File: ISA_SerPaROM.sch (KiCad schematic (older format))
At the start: 93 parts, among them J1 ISA BUS, J10 Parallel Port, J11 Serial 4 IDC, J12 Serial 3 IDC, J13 UART4_SEL, J14 ROM Config, J15 LED Bar, J2 ADDR_IRQ, J3 UART1_SEL, J4 UART2_SEL, J5 ADDR, J6 Serial 2 IDC, J7 Serial 1 DB9, J8 UART3_SEL, J9 Parport IRQ Select, U1 74HCT138, U11 74LS30, U12 74LS86, U13 74LS02, U14 74LS155, U15 74LS245, U16 74LS174, U17 74LS374, U18 74LS05, U19 74LS125, U2 74HCT138, U20 74LS240, U21 74LS244, U23 16C554, U24 74HCT32, U25 GD75232N, U26 GD75232N, U27 SST39SF040, U28 74HCT688, U5 GD75232N, U6 GD75232N, X1 1.8432Mhz

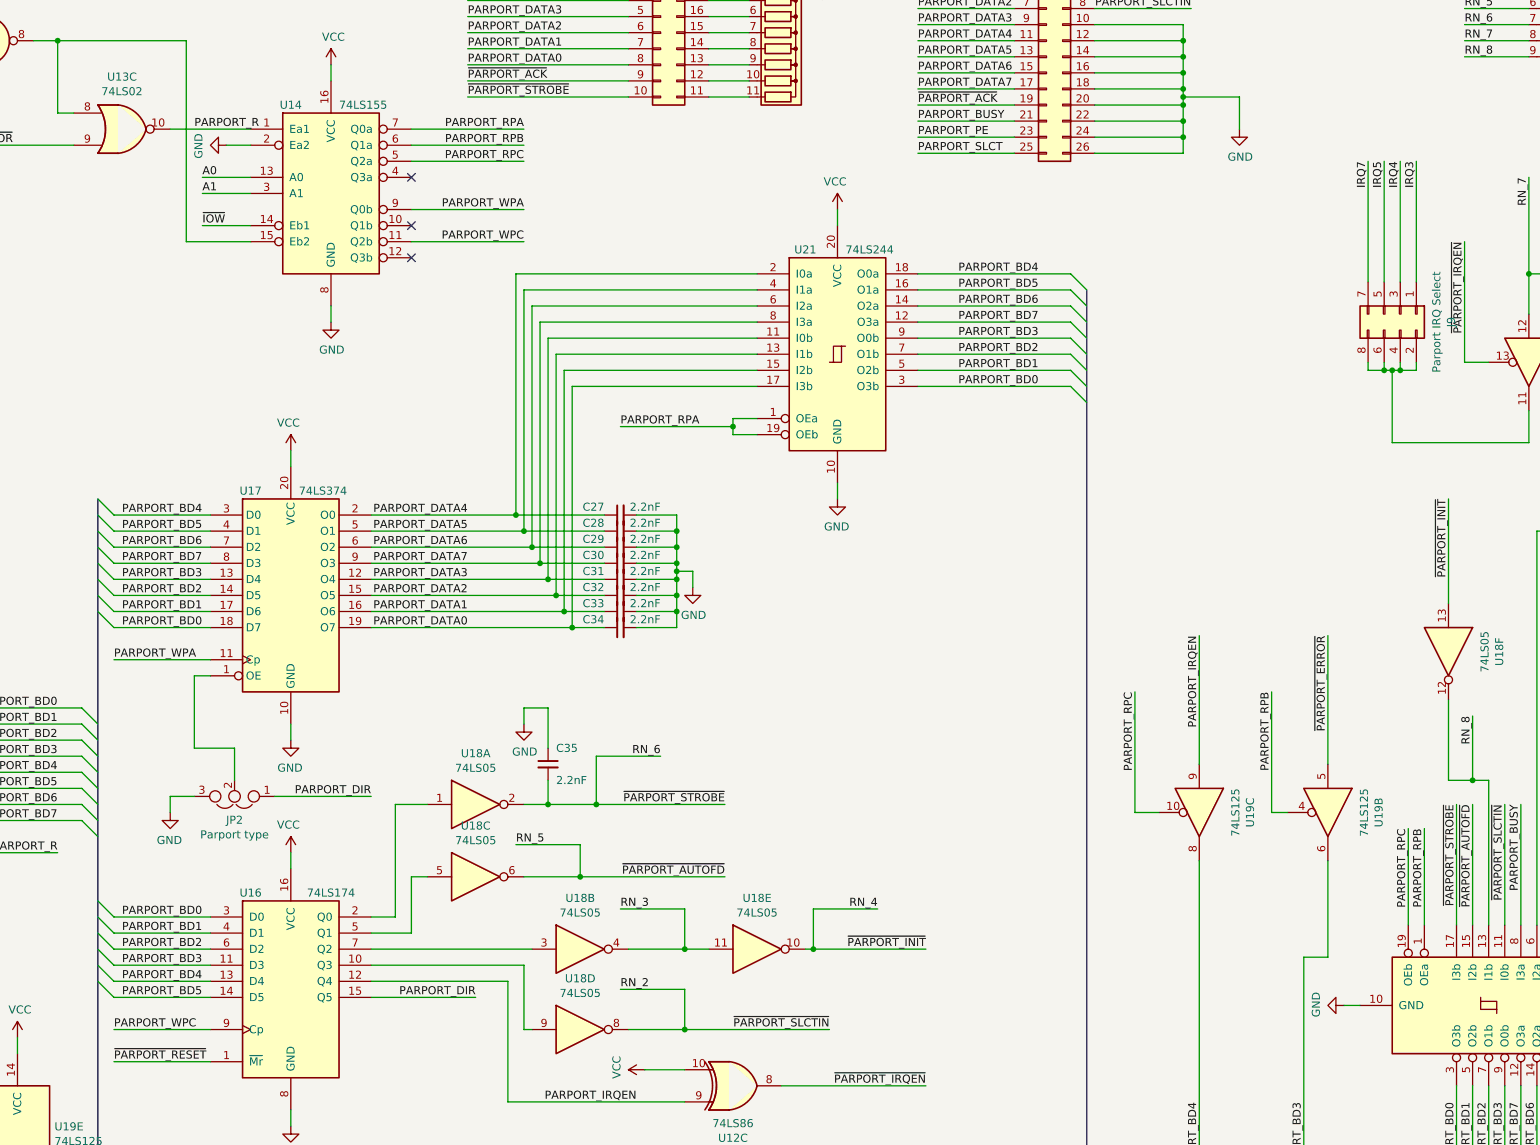
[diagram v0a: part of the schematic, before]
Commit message: Mark some active low signals as such in parport
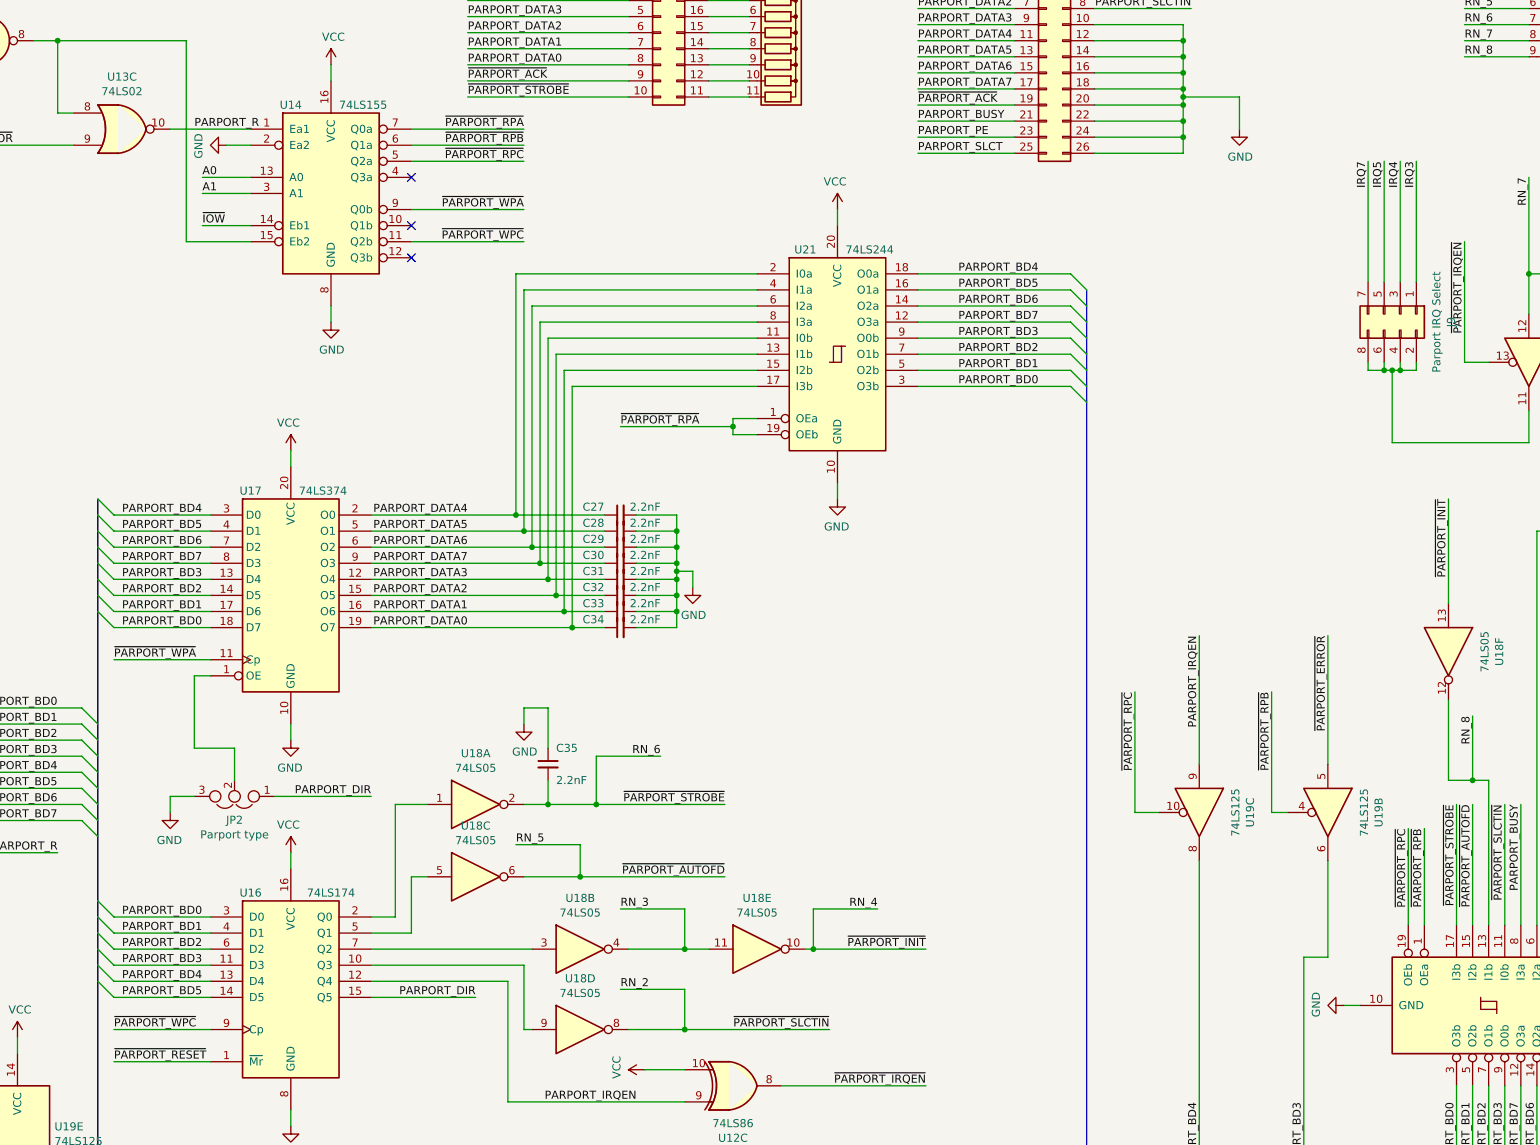
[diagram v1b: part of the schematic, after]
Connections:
- net PARPORT_RPA renamed ~PARPORT_RPA
- net PARPORT_RPB renamed ~PARPORT_RPB
- net PARPORT_RPC renamed ~PARPORT_RPC
- net PARPORT_WPA renamed ~PARPORT_WPA
- net PARPORT_WPC renamed ~PARPORT_WPC
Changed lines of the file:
@@
 NoConn ~ 9600 7600
 Text Label 10300 6800 2    50   ~ 0
-PARPORT_RPA
+~PARPORT_RPA
 Text Label 10300 6900 2    50   ~ 0
-PARPORT_RPB
+~PARPORT_RPB
 Text Label 10300 7000 2    50   ~ 0
-PARPORT_RPC
+~PARPORT_RPC
 Text Label 10300 7300 2    50   ~ 0
-PARPORT_WPA
+~PARPORT_WPA
 Text Label 10300 7500 2    50   ~ 0
-PARPORT_WPC
+~PARPORT_WPC
 $Comp
 L 74xx:74LS02 U13
@@
 	8350 12400 7750 12400
 Text Label 7750 12400 0    50   ~ 0
-PARPORT_WPC
+~PARPORT_WPC
 Wire Wire Line
 	6300 8100 6950 8100
@@
 	8350 10100 7750 10100
 Text Label 7750 10100 0    50   ~ 0
-PARPORT_WPA
+~PARPORT_WPA
 $Comp
 L Device:Jumper_NC_Dual JP2
@@
 	15900 11750 15900 11150
 Text Label 15900 11150 3    50   ~ 0
-PARPORT_RPB
+~PARPORT_RPB
 Wire Wire Line
 	15800 11750 15800 11150
 Text Label 15800 11150 3    50   ~ 0
-PARPORT_RPC
+~PARPORT_RPC
 $Comp
 L power:GND #PWR0198
@@
 	15150 13400 15050 13500
 Text Label 14950 10300 3    50   ~ 0
-PARPORT_RPB
+~PARPORT_RPB
 Wire Wire Line
 	14950 11050 15050 11050
@@
 	11600 8650 11600 8700
 Text Label 10900 8650 0    50   ~ 0
-PARPORT_RPA
+~PARPORT_RPA
 Wire Wire Line
 	12750 8400 13700 8400
@@
 $EndComp
 Text Label 14100 10300 3    50   ~ 0
-PARPORT_RPC
+~PARPORT_RPC
 Wire Wire Line
 	14100 10300 14100 11050

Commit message: Remove ROM, add buffer for uart
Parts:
- removed D1: LED Channel A, LED_THT:LED_D3.0mm-3, symbol Device:LED_Dual_CAC
- removed D2: LED Channel B, LED_THT:LED_D3.0mm-3, symbol Device:LED_Dual_CAC
- removed D3: LED Channel C, LED_THT:LED_D3.0mm-3, symbol Device:LED_Dual_CAC
- removed D4: LED Channel D, LED_THT:LED_D3.0mm-3, symbol Device:LED_Dual_CAC
- removed J14: ROM Config, Connector_PinHeader_2.54mm:PinHeader_2x07_P2.54mm_Vertical, symbol Connector_Generic:Conn_02x07_Odd_Even
- removed J15: LED Bar, Package_DIP:DIP-20_W7.62mm_Socket_LongPads, symbol Connector_Generic:Conn_02x10_Counter_Clockwise
- removed R1, R2: 10k, Resistor_THT:R_Axial_DIN0207_L6.3mm_D2.5mm_P10.16mm_Horizontal, symbol Device:R_Small
- removed R10, R3, R4, R5, R6, R7, R8, R9: 1k, Resistor_THT:R_Axial_DIN0204_L3.6mm_D1.6mm_P5.08mm_Horizontal, symbol Device:R_Small
- removed RN3: 10k, Resistor_THT:R_Array_SIP6, symbol Device:R_Network05
- removed RN4: 1.5k, Resistor_THT:R_Array_SIP11, symbol Device:R_Network10
- removed U27: SST39SF040, Package_DIP:DIP-32_W15.24mm_LongPads, symbol Memory_Flash:SST39SF040
- removed U28: 74HCT688, Package_DIP:DIP-20_W7.62mm_LongPads, symbol 74xx:74HCT688
- added C22: 100nF, Capacitor_THT:C_Disc_D6.0mm_W2.5mm_P5.00mm, symbol Device:C_Small
- added RN3: 10K, Resistor_THT:R_Array_SIP9, symbol Device:R_Network08
- added U29: 74HCT245, Package_DIP:DIP-20_W7.62mm_LongPads, symbol 74xx:74LS245
- added U30: 74HCT08, Package_DIP:DIP-14_W7.62mm_LongPads, symbol 74xx:74LS08
- RN2: value 4.7k -> 10k
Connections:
- net D0: now also U29.2 (A0); no longer U23.66 (D0)
- net D1: now also U29.3 (A1); no longer U23.67 (D1)
- net D2: now also U29.4 (A2); no longer U23.68 (D2)
- net D3: now also U29.5 (A3); no longer U23.1 (D3)
- net D4: now also U29.6 (A4); no longer U23.2 (D4)
- net D5: now also U29.7 (A5); no longer U23.3 (D5)
- net D6: now also U29.8 (A6); no longer U23.4 (D6)
- net D7: now also U29.9 (A7); no longer U23.5 (D7)
- net GND: now also C22.2, U29.10 (GND), U30.12, U30.13, U30.7 (GND)
- net VCC: now also C22.1, RN3.1 (common), U29.20 (VCC), U30.14 (VCC)
- net ~IOR: now also U29.1 (A->B)
- net ~UART1_CS: now also U30.1
- net ~UART2_CS: now also U30.2
- net ~UART3_CS: now also U30.9
- net ~UART4_CS: now also U30.10
- new net: U29.19 (CE), U30.6
- new net: U30.3, U30.4
- new net: U30.5, U30.8
- new net UART-D0: RN3.2 (R1), U23.66 (D0), U29.18 (B0)
- new net UART-D1: RN3.3 (R2), U23.67 (D1), U29.17 (B1)
- new net UART-D2: RN3.4 (R3), U23.68 (D2), U29.16 (B2)
- new net UART-D3: RN3.5 (R4), U23.1 (D3), U29.15 (B3)
- new net UART-D4: RN3.6 (R5), U23.2 (D4), U29.14 (B4)
- new net UART-D5: RN3.7 (R6), U23.3 (D5), U29.13 (B5)
- new net UART-D6: RN3.8 (R7), U23.4 (D6), U29.12 (B6)
- new net UART-D7: RN3.9 (R8), U23.5 (D7), U29.11 (B7)
- no-connect marks 37 -> 38
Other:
- note removed: "32K"
- note removed: "32K ROM bank"
- note removed: "64K"
- note removed: "64K ROM bank"
- note removed: "A000h"
- note removed: "A15"
- note removed: "A16"
- note removed: "A17"
- note removed: "A18"
- note removed: "A800h"
- note removed: "B000h"
- note removed: "B800h"
- note removed: "C000h"
- note removed: "C800h"
- note removed: "D000h"
- note removed: "D800h"
- note removed: "E000h"
- note removed: "E800h"
- note removed: "ENA"
- note removed: "F000h"
- note removed: "F800h"
- note removed: "If 32K mode is set, the A15 line will\nnot be used to address the content\nof the ROM (FLASH_A15 will be always\nlow), but will be decoded by the\n'688 to decide whether the ROM gets\nenabled or not.\n\nIn 64K mode, the A15 line will be used\nto address the content of the ROM,\nthe A15 jumper MUST be set, otherwise\nthe decoder will fail to enable the ROM\n(note how the COMPARATOR_A15 line\nwill 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"
- note removed: "Jumper ONE of these two to\nselect 32K or 64K ROM slot size"
- note removed: "Jumper to ENABLE the ROM"
- note removed: "Logic taken from https://www.lo-tech.co.uk/wiki/Lo-tech_ISA_ROM_Board"
- note removed: "ROM"
- note removed: "Remember that the comparator is\nhardwired to check for A19 to be HIGH!"
- note removed: "X"
- moved on the sheet: J11, J12, J13, J2, J3, J4, J5, J6, J7, J8, RN2, U1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

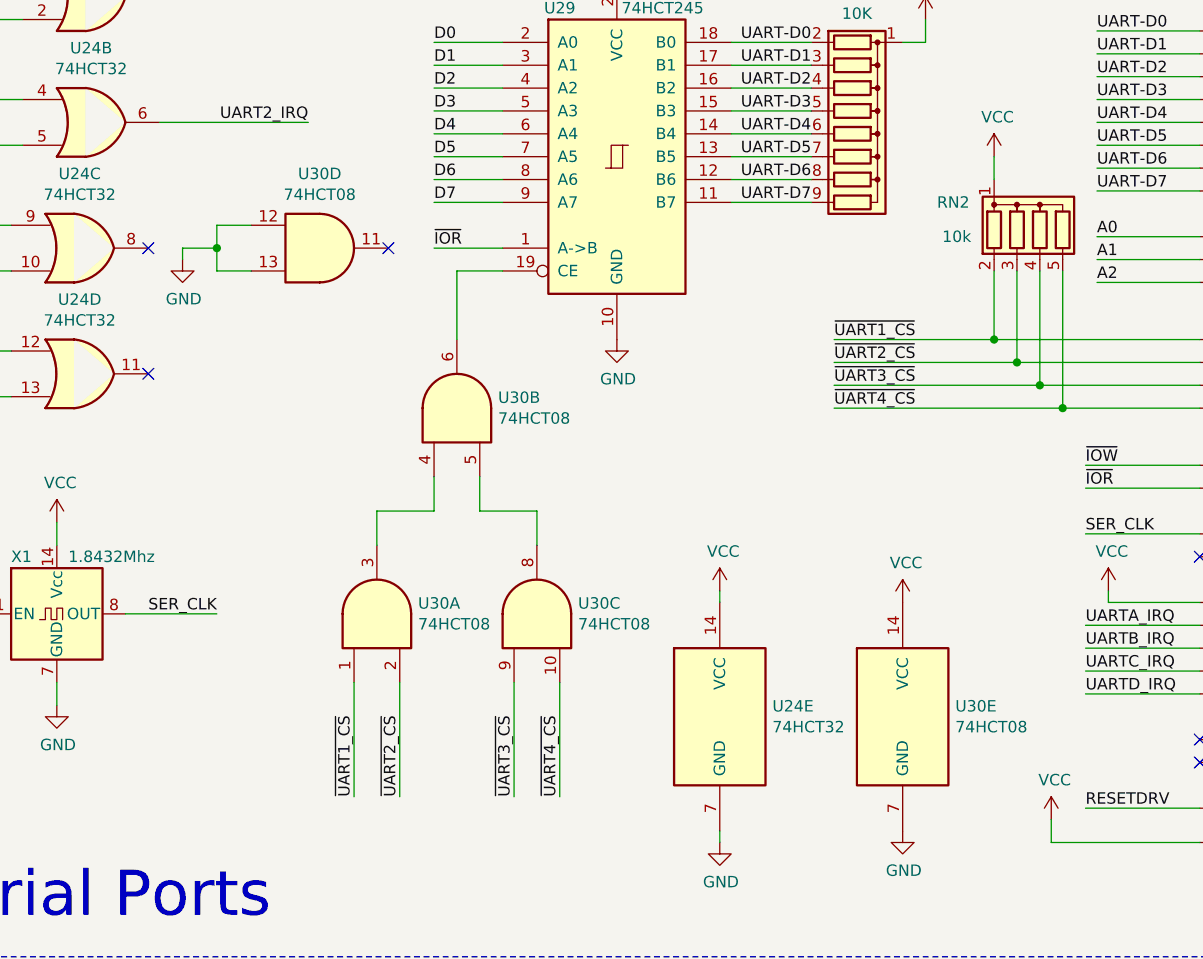
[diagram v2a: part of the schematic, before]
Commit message: Add new gerber, use 74HCT21
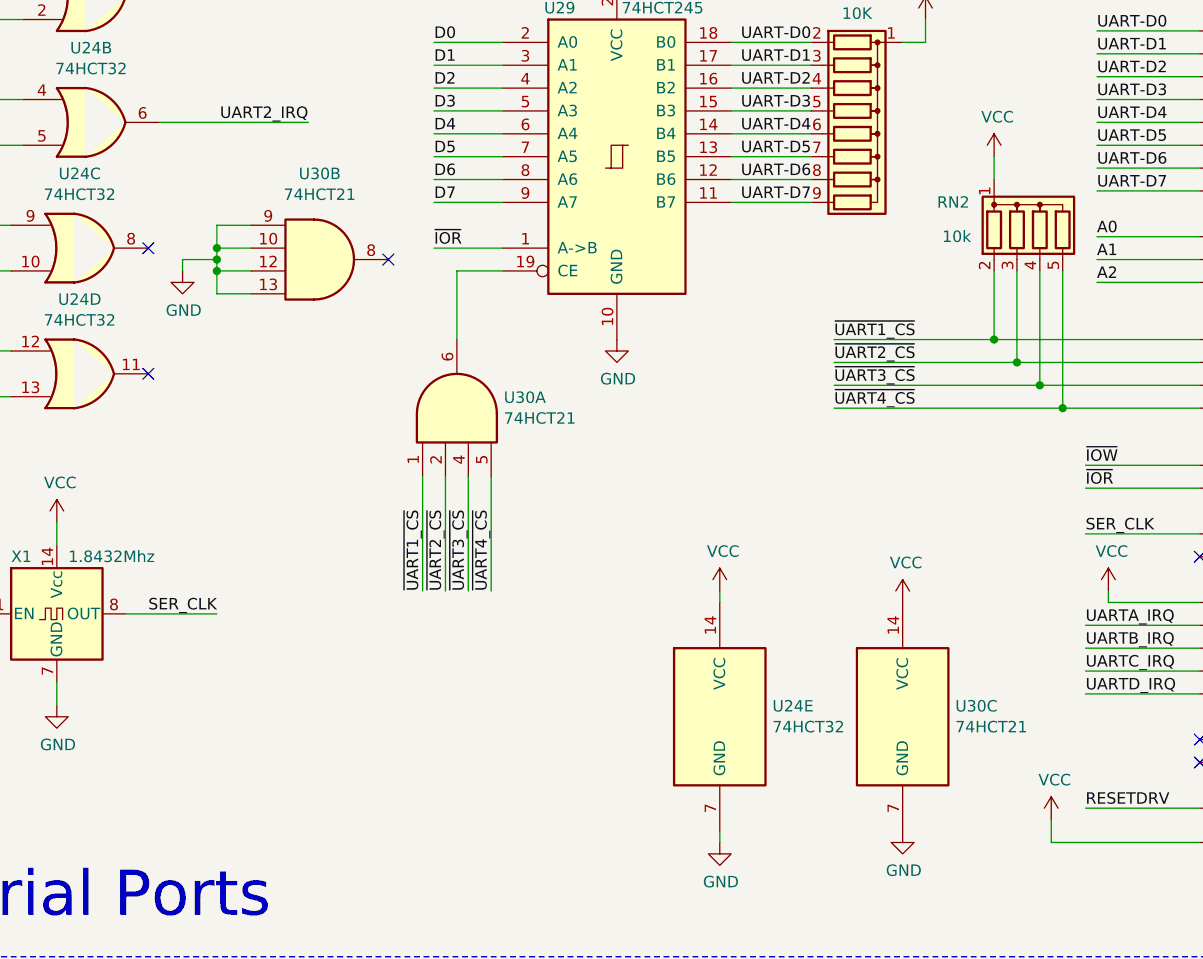
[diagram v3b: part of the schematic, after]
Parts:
- removed U30: 74HCT08, Package_DIP:DIP-14_W7.62mm_LongPads, symbol 74xx:74LS08
- added U30: 74HCT21, Package_DIP:DIP-14_W7.62mm_LongPads, symbol 74xx:74LS21
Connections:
- net GND: now also U30.10, U30.12, U30.13, U30.7 (GND), U30.9
- net VCC: now also U30.14 (VCC)
- net ~UART1_CS: now also U30.1
- net ~UART2_CS: now also U30.2
- net ~UART3_CS: now also U30.4
- net ~UART4_CS: now also U30.5
- net at U29.19 (CE): now also U30.6
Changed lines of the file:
@@
 	3450 2150 3150 2150
-$Comp
-L 74xx:74LS08 U30
-U 5 1 64A5B1AD
-P 5200 4200
-F 0 "U30" H 5430 4246 50  0000 L CNN
-F 1 "74HCT08" H 5430 4155 50  0000 L CNN
-F 2 "Package_DIP:DIP-14_W7.62mm_LongPads" H 5200 4200 50  0001 C CNN
-F 3 "http://www.ti.com/lit/gpn/sn74LS08" H 5200 4200 50  0001 C CNN
-	5    5200 4200
-	1    0    0    -1
-$EndComp
 $Comp
 L power:GND #PWR0157
@@
 	1    0    0    -1
 $EndComp
-$Comp
-L 74xx:74LS08 U30
-U 2 1 64F0BD57
-P 3250 2850
-F 0 "U30" V 3296 2670 50  0000 R CNN
-F 1 "74HCT08" V 3205 2670 50  0000 R CNN
-F 2 "Package_DIP:DIP-14_W7.62mm_LongPads" H 3250 2850 50  0001 C CNN
-F 3 "http://www.ti.com/lit/gpn/sn74LS08" H 3250 2850 50  0001 C CNN
-	2    3250 2850
-	0    -1   -1   0
-$EndComp
 Wire Wire Line
 	3450 2250 3250 2250
 Wire Wire Line
 	3250 2250 3250 2550
-$Comp
-L 74xx:74LS08 U30
-U 1 1 653A42F4
-P 2900 3750
-F 0 "U30" V 2946 3570 50  0000 R CNN
-F 1 "74HCT08" V 2855 3570 50  0000 R CNN
-F 2 "Package_DIP:DIP-14_W7.62mm_LongPads" H 2900 3750 50  0001 C CNN
-F 3 "http://www.ti.com/lit/gpn/sn74LS08" H 2900 3750 50  0001 C CNN
-	1    2900 3750
-	0    -1   -1   0
-$EndComp
-$Comp
-L 74xx:74LS08 U30
-U 3 1 653A674A
-P 3600 3750
-F 0 "U30" V 3646 3570 50  0000 R CNN
-F 1 "74HCT08" V 3555 3570 50  0000 R CNN
-F 2 "Package_DIP:DIP-14_W7.62mm_LongPads" H 3600 3750 50  0001 C CNN
-F 3 "http://www.ti.com/lit/gpn/sn74LS08" H 3600 3750 50  0001 C CNN
-	3    3600 3750
-	0    -1   -1   0
-$EndComp
-$Comp
-L 74xx:74LS08 U30
-U 4 1 654CAC9F
-P 2650 2150
-F 0 "U30" H 2650 2475 50  0000 C CNN
-F 1 "74HCT08" H 2650 2384 50  0000 C CNN
-F 2 "Package_DIP:DIP-14_W7.62mm_LongPads" H 2650 2150 50  0001 C CNN
-F 3 "http://www.ti.com/lit/gpn/sn74LS08" H 2650 2150 50  0001 C CNN
-	4    2650 2150
-	1    0    0    -1
-$EndComp
-NoConn ~ 2950 2150
 Wire Wire Line
 	2350 2050 2200 2050
@@
 L power:GND #PWR0159
 U 1 1 6583E940
-P 2050 2200
-F 0 "#PWR0159" H 2050 1950 50  0001 C CNN
-F 1 "GND" H 2055 2027 50  0000 C CNN
-F 2 "" H 2050 2200 50  0001 C CNN
-F 3 "" H 2050 2200 50  0001 C CNN
-	1    2050 2200
-	1    0    0    -1
-$EndComp
-Wire Wire Line
-	2050 2200 2050 2150
-Wire Wire Line
-	2050 2150 2200 2150
+P 2050 2250
+F 0 "#PWR0159" H 2050 2000 50  0001 C CNN
+F 1 "GND" H 2055 2077 50  0000 C CNN
+F 2 "" H 2050 2250 50  0001 C CNN
+F 3 "" H 2050 2250 50  0001 C CNN
+	1    2050 2250
+	1    0    0    -1
+$EndComp
+Wire Wire Line
+	2050 2250 2050 2200
+Wire Wire Line
+	2050 2200 2200 2200
 Connection ~ 2200 2150
 Wire Wire Line
-	2200 2150 2200 2250
-Wire Wire Line
-	2900 3450 2900 3300
-Wire Wire Line
-	2900 3300 3150 3300
-Wire Wire Line
-	3150 3300 3150 3150
-Wire Wire Line
-	3600 3450 3600 3300
-Wire Wire Line
-	3600 3300 3350 3300
-Wire Wire Line
-	3350 3300 3350 3150
-Wire Wire Line
-	2800 4050 2800 4550
-Text Label 2800 4550 1    50   ~ 0
+	2200 2150 2200 2200
+Wire Wire Line
+	3100 3150 3100 3650
+Text Label 3100 3650 1    50   ~ 0
 ~UART1_CS
 Wire Wire Line
-	3000 4050 3000 4550
-Text Label 3000 4550 1    50   ~ 0
+	3200 3150 3200 3650
+Text Label 3200 3650 1    50   ~ 0
 ~UART2_CS
 Wire Wire Line
-	3500 4050 3500 4550
-Text Label 3500 4550 1    50   ~ 0
-~UART3_CS
-Wire Wire Line
-	3700 4050 3700 4550
-Text Label 3700 4550 1    50   ~ 0
+	3400 3150 3400 3650
+Text Label 3400 3650 1    50   ~ 0
 ~UART4_CS
 $Comp
@@
 Wire Wire Line
 	4250 14400 3850 14400
+Connection ~ 3850 14400
+$Comp
+L 74xx:74LS21 U30
+U 3 1 60632836
+P 5200 4200
+F 0 "U30" H 5430 4246 50  0000 L CNN
+F 1 "74HCT21" H 5430 4155 50  0000 L CNN
+F 2 "Package_DIP:DIP-14_W7.62mm_LongPads" H 5200 4200 50  0001 C CNN
+F 3 "http://www.ti.com/lit/gpn/sn74LS21" H 5200 4200 50  0001 C CNN
+	3    5200 4200
+	1    0    0    -1
+$EndComp
+$Comp
+L 74xx:74LS21 U30
+U 1 1 6071A691
+P 3250 2850
+F 0 "U30" V 3296 2645 50  0000 R CNN
+F 1 "74HCT21" V 3205 2645 50  0000 R CNN
+F 2 "Package_DIP:DIP-14_W7.62mm_LongPads" H 3250 2850 50  0001 C CNN
+F 3 "http://www.ti.com/lit/gpn/sn74LS21" H 3250 2850 50  0001 C CNN
+	1    3250 2850
+	0    -1   -1   0
+$EndComp
+Text Label 3300 3650 1    50   ~ 0
+~UART3_CS
+Wire Wire Line
+	3300 3150 3300 3650
+$Comp
+L 74xx:74LS21 U30
+U 2 1 610C1C2C
+P 2650 2200
+F 0 "U30" H 2650 2575 50  0000 C CNN
+F 1 "74HCT21" H 2650 2484 50  0000 C CNN
+F 2 "Package_DIP:DIP-14_W7.62mm_LongPads" H 2650 2200 50  0001 C CNN
+F 3 "http://www.ti.com/lit/gpn/sn74LS21" H 2650 2200 50  0001 C CNN
+	2    2650 2200
+	1    0    0    -1
+$EndComp
+NoConn ~ 2950 2200
+Wire Wire Line
+	2200 2150 2350 2150
+Wire Wire Line
+	2200 2250 2200 2350
+Wire Wire Line
+	2200 2350 2350 2350
+Connection ~ 2200 2250
+Connection ~ 2200 2200
+Wire Wire Line
+	2200 2200 2200 2250
 Wire Bus Line
 	13800 7800 13800 13500
@@
 Wire Bus Line
 	7650 9100 7650 13500
-Connection ~ 3850 14400
 $EndSCHEMATC
